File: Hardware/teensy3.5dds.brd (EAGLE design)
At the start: 111.5 x 90.9 mm, 98 parts, among them IC1 AD8034, IC10 AD8034, IC11 AD8034, IC12 AD8034, IC2 AD8034, IC4 AD737KRZ-R7, IC8 AD8034, IC9 AD8034, J1 1776275-2, J2 1776275-2, Q1 CSM-7X-DU, X1 1-227161-0

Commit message: hardware: board v0.3 could it by shrinked a little bit on the shorter side?
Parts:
- added C32, C35: 100n, rcl:C0805
- added C34: 100n, rcl:C1206
- C7: value 100n 16V -> 1u; device rcl:C0805 -> rcl:C1206
- C8: value 1uF 16V -> 1u; device rcl:085CS_1AR -> rcl:C0805
- moved C7 5.71 mm to (7.62, 69.3)
- moved C8 2.34 mm to (8.13, 65.8), turned to 0 degrees
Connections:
- net +5V: now also C32.1, C34.1, C35.1, C8.1; no longer C8.+
- net GND: now also C32.2, C34.2, C35.2, C8.2, U$2.15, U$2.35, U$2.43; no longer C8.-
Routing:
- net GND: track 796.0 -> 862.1 mm, vias 16 -> 18
- net +5V: track 280.3 -> 296.2 mm
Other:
- board text added: "FILTERED"
- board text added: "NOT FILTERED"

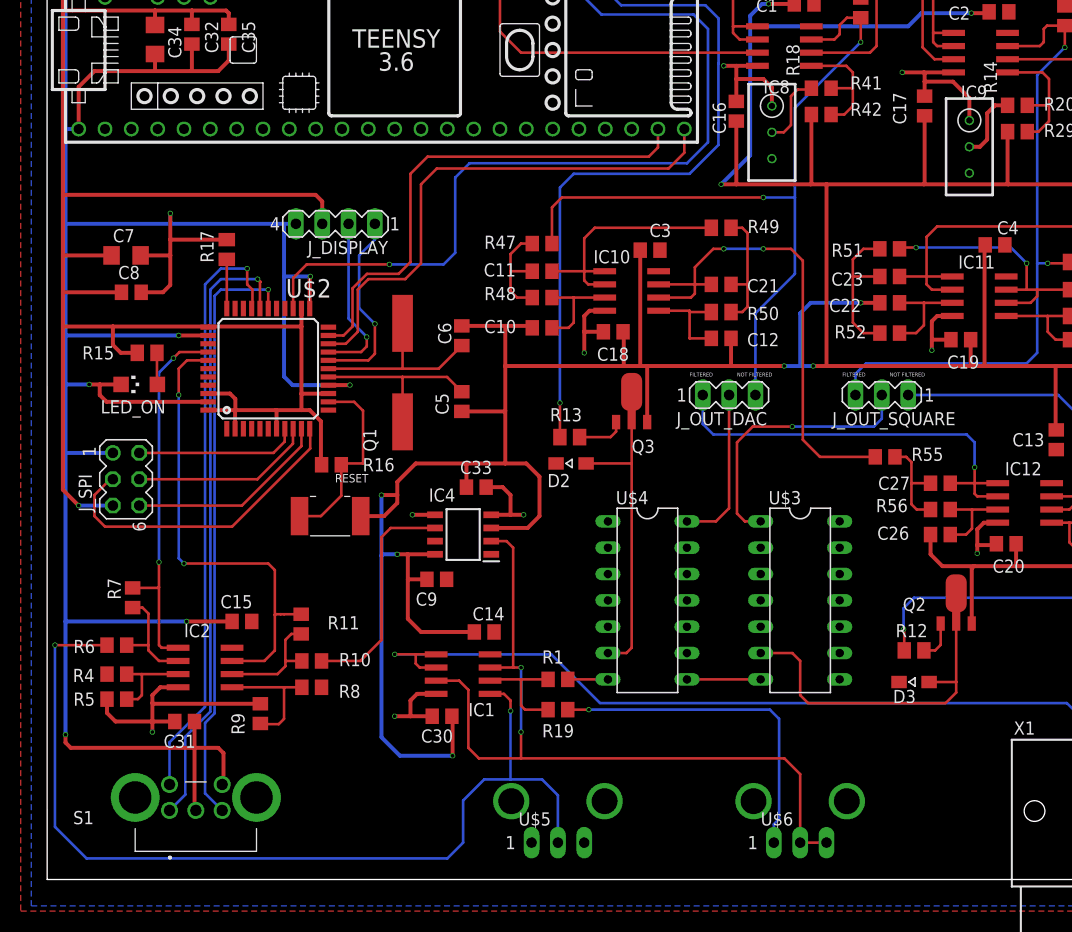
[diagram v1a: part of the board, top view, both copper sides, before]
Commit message: hardware: board v0.4 add M4 mounting holes
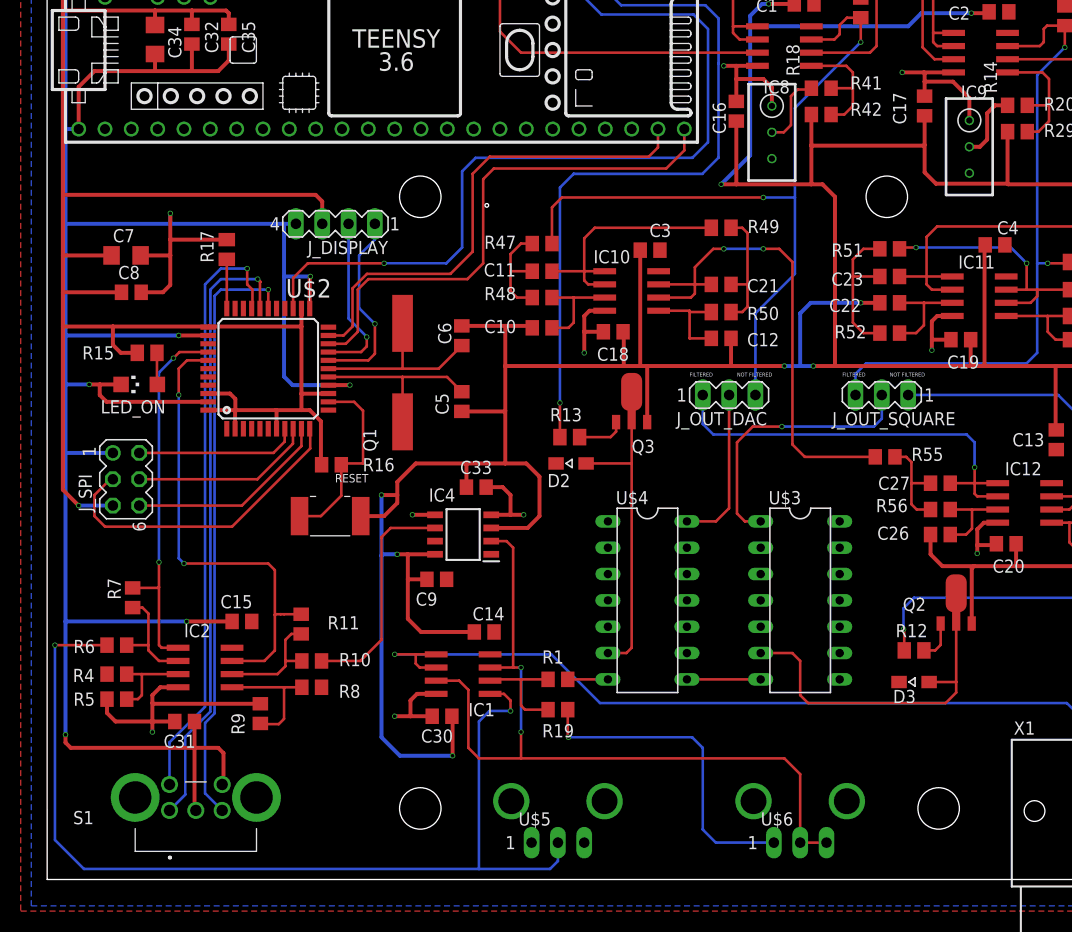
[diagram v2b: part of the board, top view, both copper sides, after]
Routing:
- net N$3: track 92.9 -> 96.5 mm
- net N$15: track 32.9 -> 31.3 mm
- net GND: track 862.1 -> 862.9 mm
- net DAC0_SEL: track 67.1 -> 67.9 mm
- net TX1: track 48.2 -> 47.6 mm

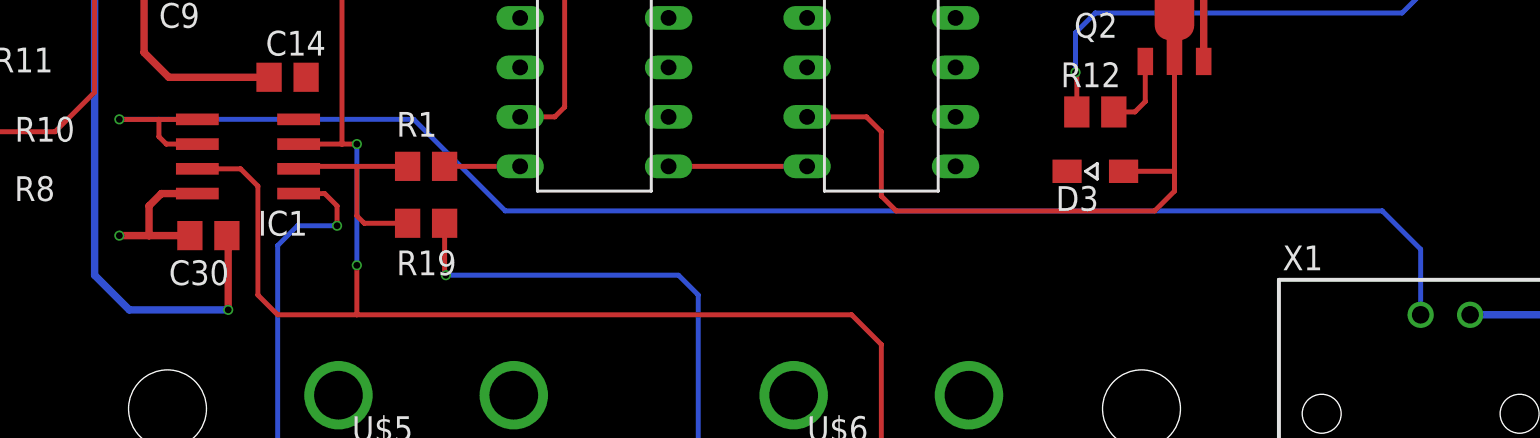
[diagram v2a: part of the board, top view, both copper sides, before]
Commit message: hardware: add 50 Ohm resistor before BNC connector
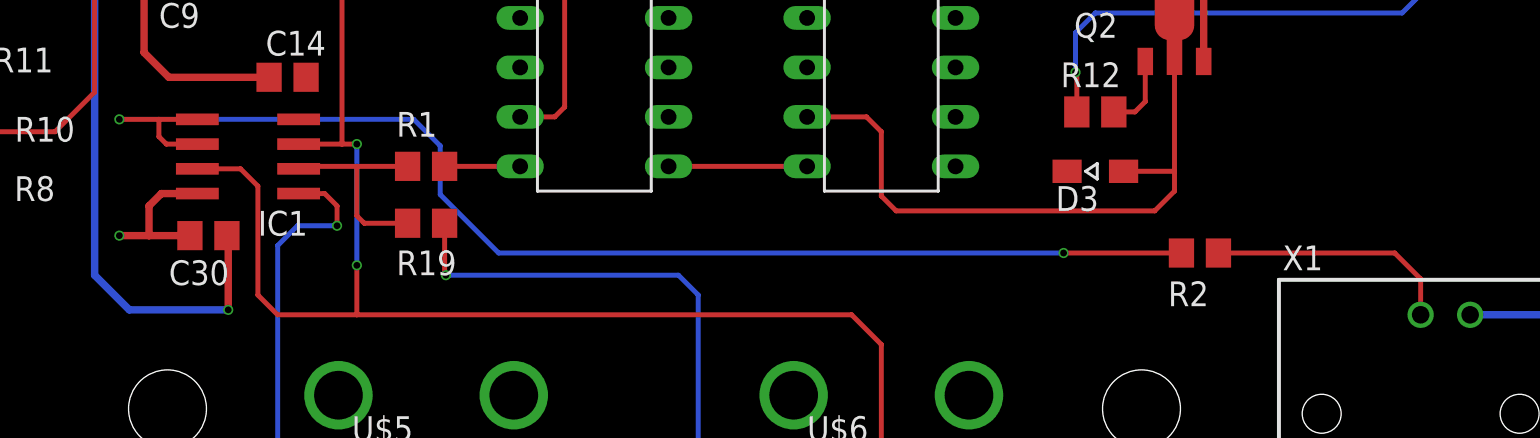
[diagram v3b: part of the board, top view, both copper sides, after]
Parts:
- added R2: (no value), rcl:R0805
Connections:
- new net N$6: R2.2, X1.1
- net N$19: now also R2.1; no longer X1.1
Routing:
- net N$19: track 80.0 -> 65.9 mm, vias 1 -> 2
- net N$6: track 0.00 -> 12.8 mm
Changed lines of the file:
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@@
 <attribute name="SPICEPREFIX" value="C" x="8.128" y="65.786" size="1.778" layer="27" display="off"/>
+</element>
+<element name="R2" library="rcl" library_urn="urn:adsk.eagle:library:334" package="R0805" package3d_urn="urn:adsk.eagle:package:23553/2" value="" x="89" y="24" smashed="yes">
+<attribute name="NAME" x="87.365" y="21.27" size="1.27" layer="25"/>
+<attribute name="POPULARITY" value="86" x="89" y="24" size="1.778" layer="27" display="off"/>
+<attribute name="SPICEPREFIX" value="R" x="89" y="24" size="1.778" layer="27" display="off"/>
+<attribute name="VALUE" x="88.365" y="21.46" size="1.27" layer="27"/>
 </element>
 </elements>
@@
 <signal name="N$19" class="1">
 <contactref element="IC1" pad="2"/>
-<contactref element="X1" pad="1"/>
 <contactref element="IC1" pad="1"/>
-<wire x1="48.641" y1="30.861" x2="53.34" y2="26.162" width="0.254" layer="16"/>
-<wire x1="100.33" y1="20.828" x2="100.33" y2="24.1935" width="0.254" layer="16"/>
-<wire x1="100.33" y1="24.1935" x2="98.3615" y2="26.162" width="0.254" layer="16"/>
-<wire x1="53.34" y1="26.162" x2="98.3615" y2="26.162" width="0.254" layer="16"/>
 <via x="33.528" y="30.861" extent="1-16" drill="0.35"/>
 <wire x1="37.532" y1="29.591" x2="35.941" y2="29.591" width="0.254" layer="1"/>
 <wire x1="35.941" y1="29.591" x2="35.56" y2="29.972" width="0.254" layer="1"/>
-<wire x1="48.641" y1="30.861" x2="33.528" y2="30.861" width="0.254" layer="16"/>
+<wire x1="33.528" y1="30.861" x2="48.641" y2="30.861" width="0.254" layer="16"/>
 <wire x1="33.528" y1="30.861" x2="35.56" y2="30.861" width="0.254" layer="1"/>
 <wire x1="35.56" y1="30.861" x2="37.532" y2="30.861" width="0.254" layer="1"/>
 <wire x1="35.56" y1="29.972" x2="35.56" y2="30.861" width="0.254" layer="1"/>
+<contactref element="R2" pad="1"/>
+<wire x1="48.641" y1="30.861" x2="50" y2="29.502" width="0.254" layer="16"/>
+<wire x1="53" y1="24" x2="82" y2="24" width="0.254" layer="16"/>
+<via x="82" y="24" extent="1-16" drill="0.35"/>
+<wire x1="50" y1="29.502" x2="50" y2="27" width="0.254" layer="16"/>
+<wire x1="50" y1="27" x2="53" y2="24" width="0.254" layer="16"/>
+<wire x1="82" y1="24" x2="88.05" y2="24" width="0.254" layer="1"/>
+</signal>
+<signal name="N$6" class="1">
+<contactref element="X1" pad="1"/>
+<contactref element="R2" pad="2"/>
+<wire x1="100.33" y1="22.67" x2="100.33" y2="20.828" width="0.254" layer="1"/>
+<wire x1="89.95" y1="24" x2="99" y2="24" width="0.254" layer="1"/>
+<wire x1="99" y1="24" x2="100.33" y2="22.67" width="0.254" layer="1"/>
 </signal>
 </signals>

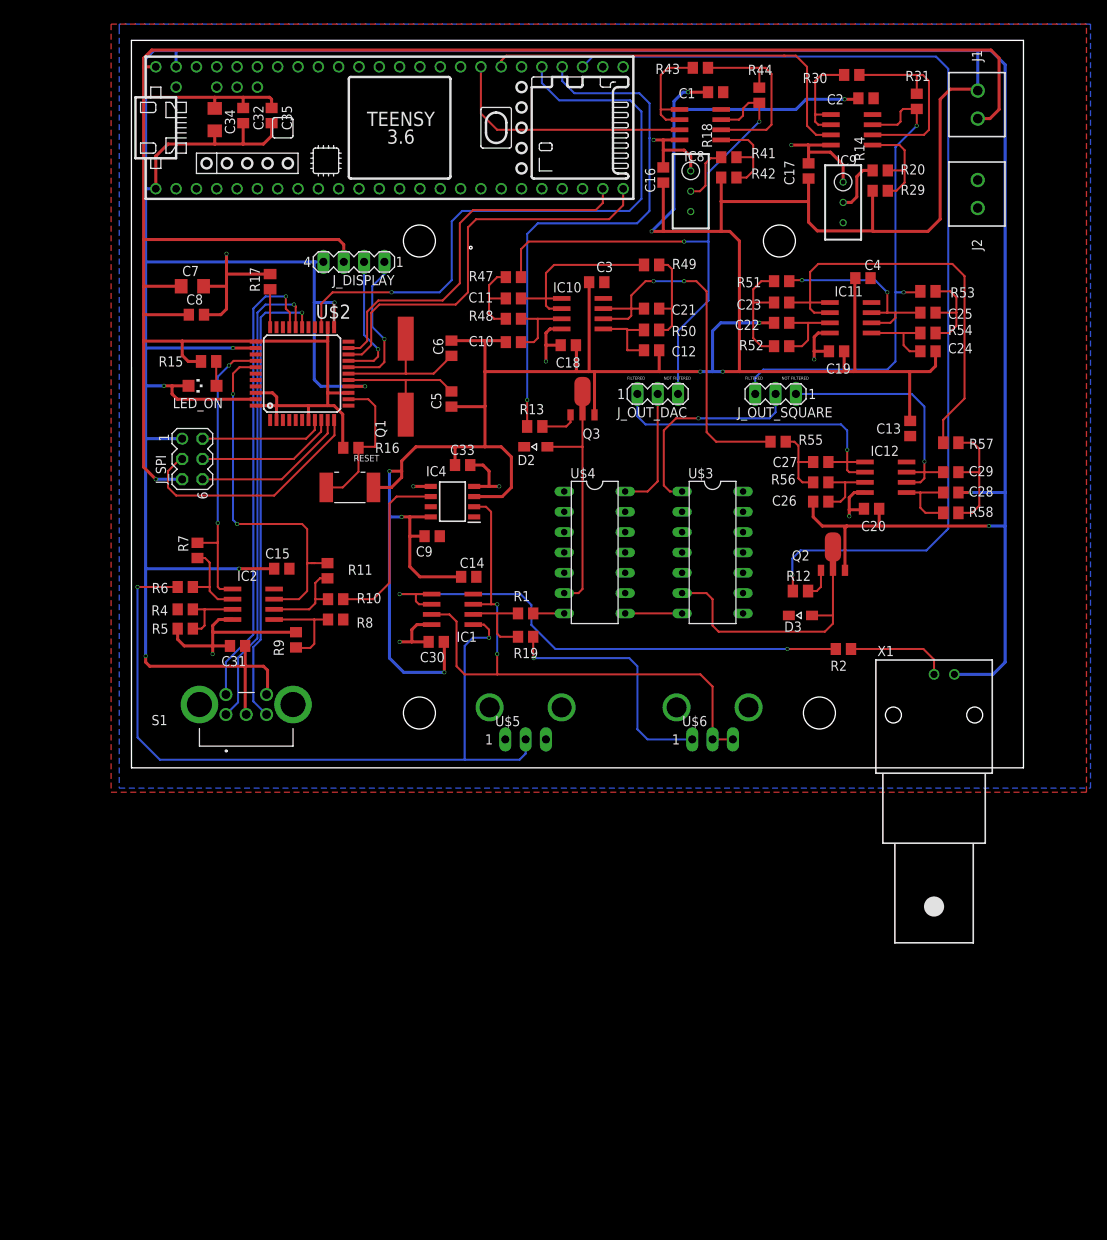
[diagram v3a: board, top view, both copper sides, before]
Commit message: hardware: board v0.5 * shrink down to 11*8.5cm * Correct a few derps * Cumulative of caps changes on teensy and 32u4, add writes to output type choosing * Ignore overlap on transistors * Ignore AirWire on U4 and U3 (PRME15005) since the pins are shorted
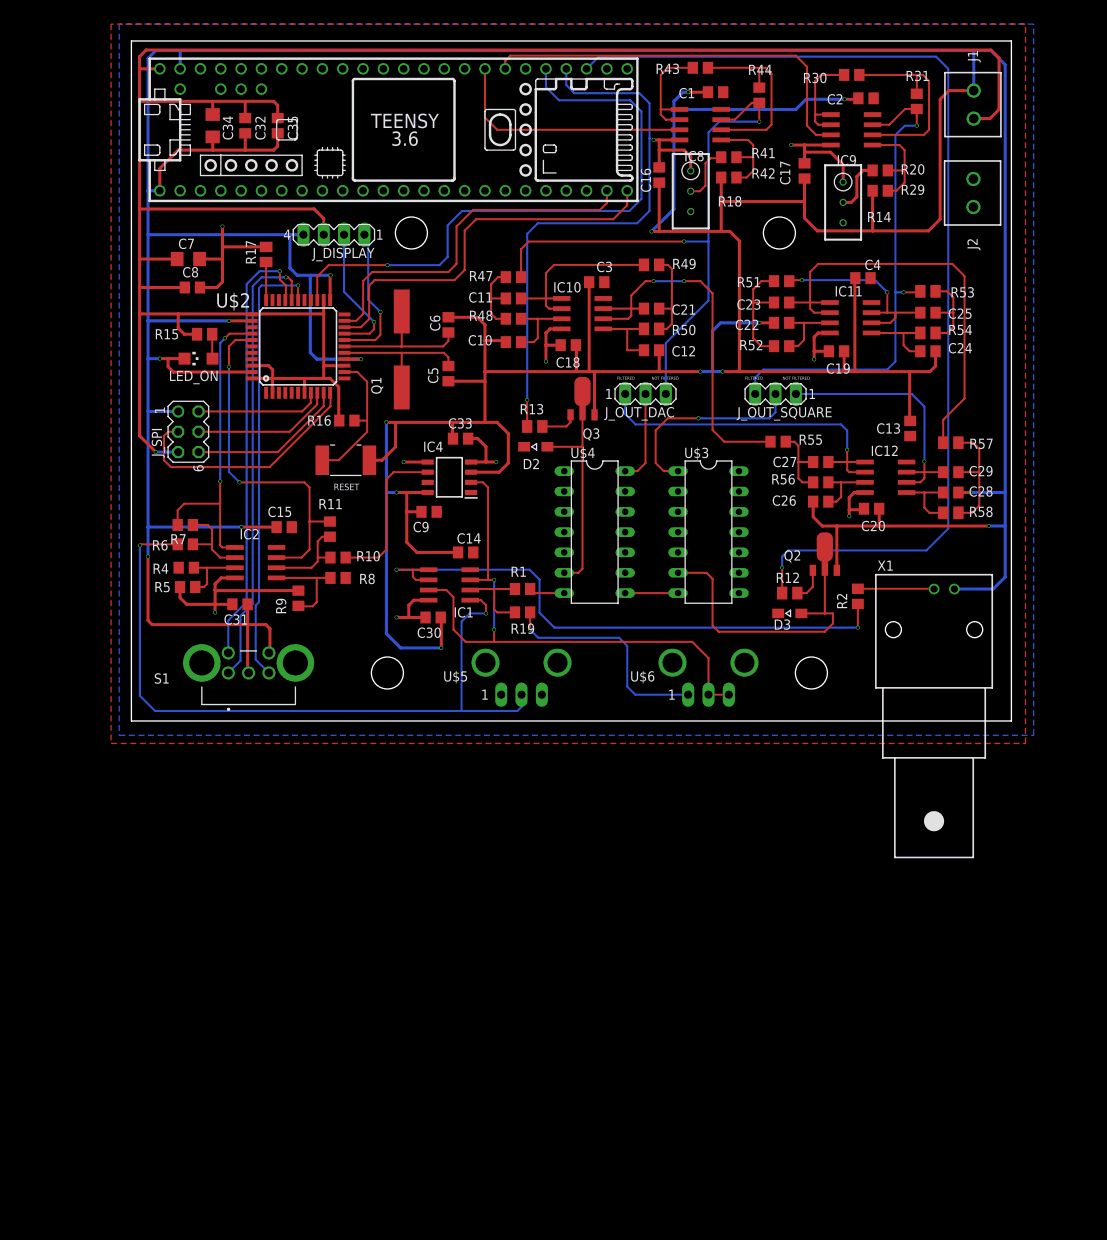
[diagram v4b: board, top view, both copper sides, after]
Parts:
- moved X1 10.7 mm to (100.3, 26.4)
- moved R2 6.82 mm to (90.8, 30.6), turned to 90 degrees
- moved U$6 5.61 mm to (72.1, 18.3)
- moved U$5 5.61 mm to (48.8, 18.3)
- moved R6 5.33 mm to (6.73, 37.1)
- moved R10 5.21 mm to (25.8, 35.4)
- moved R11 5.21 mm to (24.8, 39.0)
- moved R8 5.21 mm to (25.8, 32.9)
- moved S1 5.21 mm to (14.7, 20.1)
- moved C31 5.21 mm to (13.6, 29.6)
- moved R5 5.21 mm to (7.03, 31.7)
- moved R9 5.21 mm to (20.9, 30.3)
- moved C15 5.21 mm to (19.1, 39.2)
- moved IC2 5.21 mm to (15.5, 34.8)
- moved R4 5.21 mm to (6.86, 34.2)
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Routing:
- net GND: track 862.9 -> 844.5 mm
- net N$19: track 65.9 -> 73.1 mm
- net N$3: track 96.5 -> 91.7 mm
- net N$2: track 32.7 -> 37.1 mm
- net N$9: track 76.9 -> 72.7 mm
- net DAC0_OUT: track 15.5 -> 11.6 mm
- net INTERRUPT: track 79.6 -> 76.2 mm
- net N$6: track 12.8 -> 9.54 mm
- net N$15: track 31.3 -> 28.3 mm
- net DAC0_OFFSET: track 74.1 -> 77.1 mm
- net OFF_MEASURE: track 36.4 -> 39.2 mm
- net N$25: track 58.4 -> 55.8 mm
- net N$12: track 28.9 -> 26.4 mm
- net RX1: track 51.3 -> 48.8 mm
- net N$8: track 59.8 -> 57.5 mm
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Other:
- board size 111.5 x 90.9 mm -> 110 x 85 mm
